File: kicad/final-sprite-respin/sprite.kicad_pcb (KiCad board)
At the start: 4 copper layers, 35 x 35 mm, 70 parts, among them J1 M20-7910442R, U1 CC430F513X, U2 LSM9DS1, U3 SPRITETCXO_TCXO_7Z, U4 DRV8837, U5 ADP5092, U6 DRV8837, U7 DRV8837, U8 TASC, U9 TASC, X1 SPRITEPIN_SPRITE_PIN, X2 SPRITEPIN_SPRITE_PIN

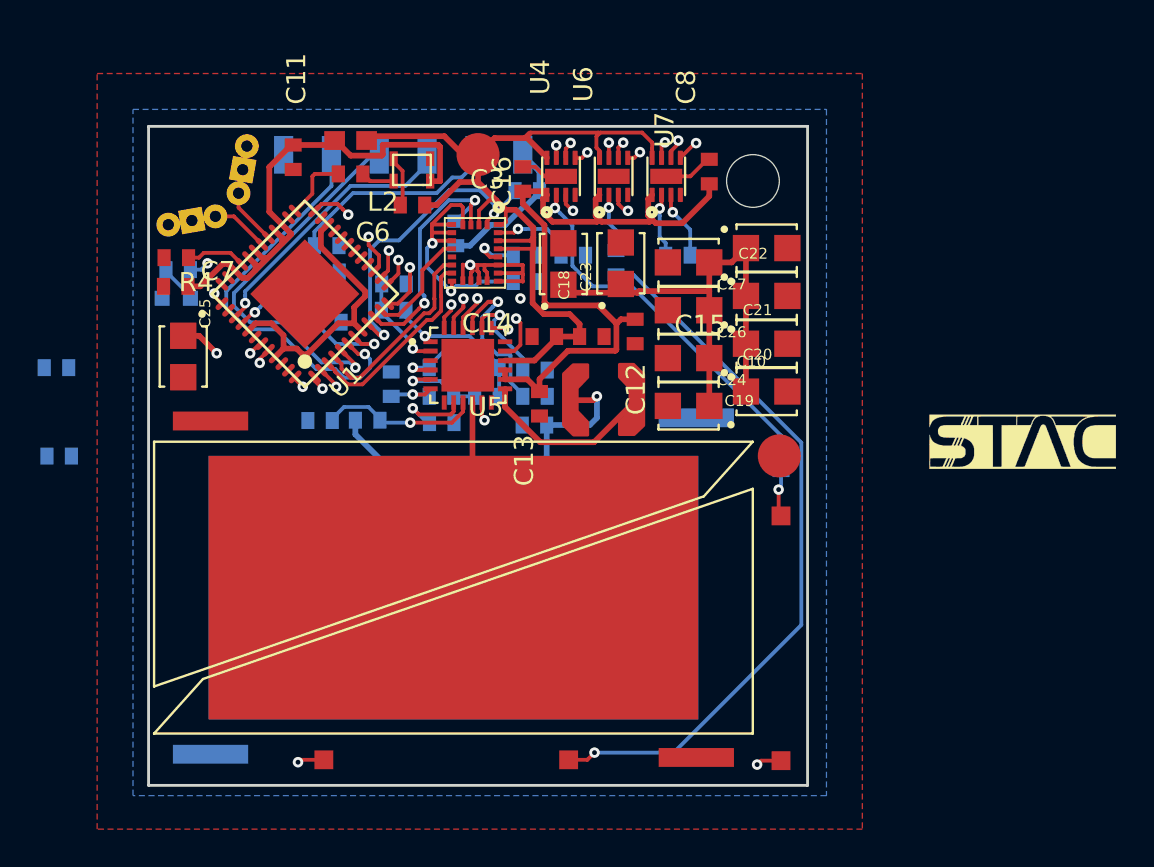
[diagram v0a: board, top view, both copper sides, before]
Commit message: Cap board repsin with all nets connected
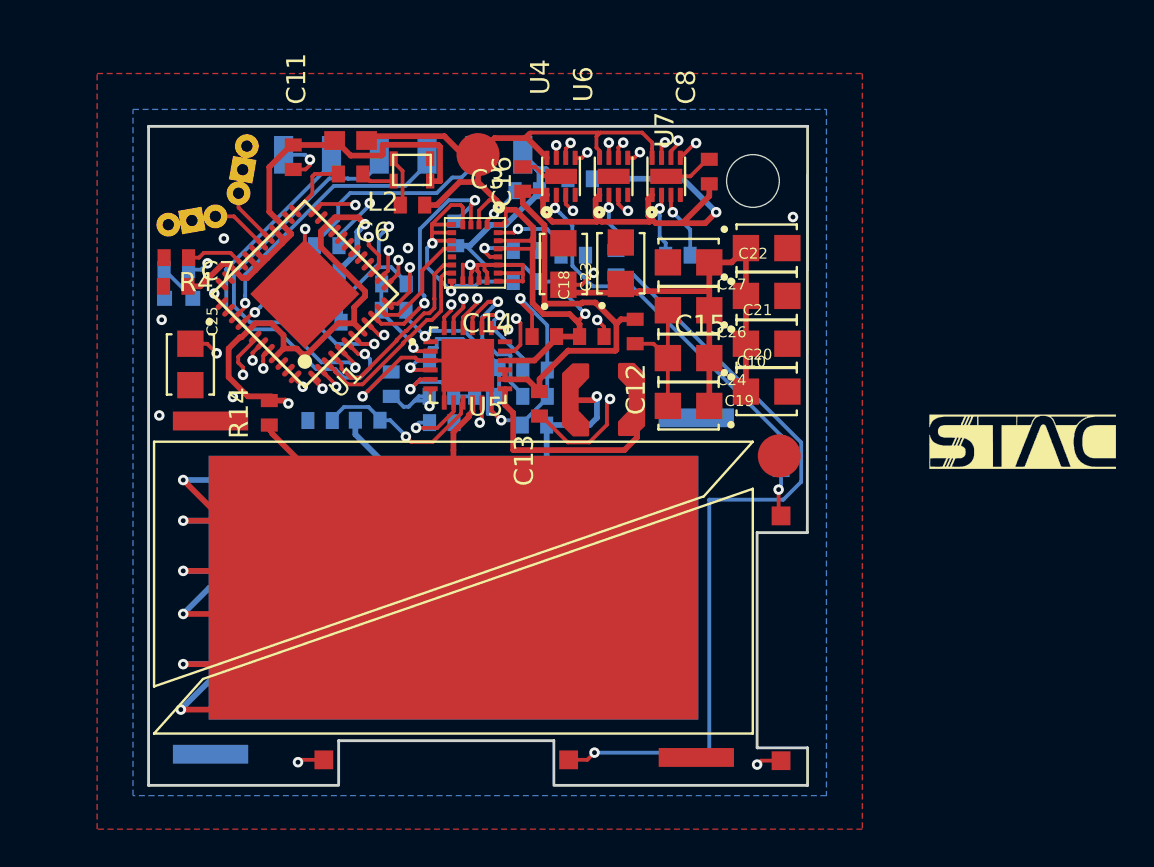
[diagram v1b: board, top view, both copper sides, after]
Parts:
- R14: moved to F.Cu
- moved R13 31.3 mm to (143.8, 86.2)
- moved R14 11.6 mm to (127.3, 98.7), turned to 270 degrees
- moved C25 0.57 mm to (123.1, 96.1)
- moved R21 0.38 mm to (136.4, 95.9)
- moved C4 0.25 mm to (140.9, 90.0)
- moved LED1 0.13 mm to (122.4, 92.6)
- moved R2 0.10 mm to (122.3, 91.1)
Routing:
- net VCCINT: track 38.9 -> 243.3 mm, vias 1 -> 7
- net GND: track 17.9 -> 83.2 mm, vias 2 -> 17
- net VCC: track 71.3 -> 112.9 mm, vias 0 -> 3
- net /VBAT: track 53.5 -> 64.0 mm, vias 2 -> 3
- net VCCIO: track 37.0 -> 46.6 mm, vias 0 -> 1
- net /PGOOD: track 3.65 -> 10.6 mm
- net /PWM2: track 40.3 -> 44.0 mm
- net /PWM1: track 44.3 -> 47.8 mm
- net Net-(L4-Pad1): track 38.5 -> 41.9 mm
- net /SWN: track 9.70 -> 12.3 mm
- net /SCL: track 16.8 -> 14.6 mm
- net /TERM: track 5.24 -> 6.98 mm
- net /SETHYS: track 3.29 -> 4.45 mm
- net /UART_TX: track 20.5 -> 21.4 mm
- net Net-(R7-Pad1): track 8.47 -> 9.34 mm
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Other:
- outline, holes or cut-outs redrawn

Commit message: Fix edge cuts
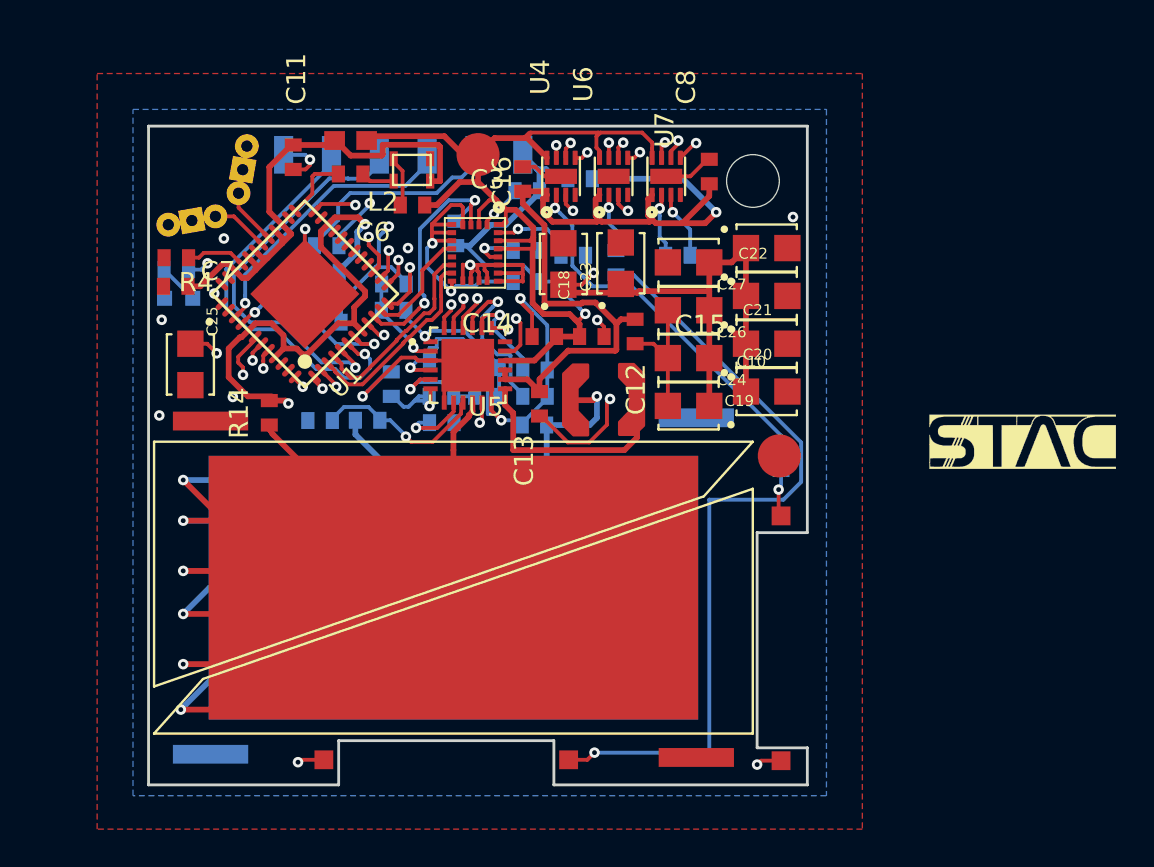
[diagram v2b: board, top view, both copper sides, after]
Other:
- outline, holes or cut-outs redrawn
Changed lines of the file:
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@@
-(kicad_pcb (version 20171130) (host pcbnew "(5.0.0-3-g5ebb6b6)")
+(kicad_pcb (version 20171130) (host pcbnew 6.0.0-rc1-unknown)
   (general
     (thickness 0.7874)
@@
     (2 Route3 signal)
     (31 Bottom signal)
-    (32 B.Adhes user hide)
+    (32 B.Adhes user)
     (33 F.Adhes user)
-    (34 B.Paste user hide)
-    (35 F.Paste user hide)
+    (34 B.Paste user)
+    (35 F.Paste user)
     (36 B.SilkS user)
     (37 F.SilkS user)
-    (38 B.Mask user hide)
-    (39 F.Mask user hide)
-    (40 Dwgs.User user hide)
-    (41 Cmts.User user hide)
-    (42 Eco1.User user hide)
-    (43 Eco2.User user hide)
+    (38 B.Mask user)
+    (39 F.Mask user)
+    (40 Dwgs.User user)
+    (41 Cmts.User user)
+    (42 Eco1.User user)
+    (43 Eco2.User user)
     (44 Edge.Cuts user)
-    (45 Margin user hide)
+    (45 Margin user)
     (46 B.CrtYd user)
     (47 F.CrtYd user)
-    (48 B.Fab user hide)
+    (48 B.Fab user)
     (49 F.Fab user)
   )
@@
     (zone_45_only no)
     (trace_min 0.1524)
-    (segment_width 0.15)
-    (edge_width 0.15)
     (via_size 0.5588)
     (via_drill 0.254)
@@
     (uvia_min_size 0.2)
     (uvia_min_drill 0.1)
+    (edge_width 0.15)
+    (segment_width 0.15)
     (pcb_text_width 0.3)
     (pcb_text_size 1.5 1.5)
@@
     (uvia_dia 25.4)
     (uvia_drill 12.7)
+    (diff_pair_width 0.1524)
     (diff_pair_gap 0.1524)
-    (diff_pair_width 0.1524)
     (add_net /DRDY)
     (add_net /DSW)
@@
     (uvia_dia 25.4)
     (uvia_drill 12.7)
+    (diff_pair_width 0.1524)
     (diff_pair_gap 0.1524)
-    (diff_pair_width 0.1524)
     (add_net /SWN)
     (add_net /VBAT)
@@
     (pad "" np_thru_hole circle (at 0 0) (size 2.8 2.8) (drill 2.8) (layers *.Cu *.Mask))
   )
-  (gr_line (start 130.937 118.452074) (end 120.8411 118.452074) (layer Edge.Cuts) (width 0.15))
-  (gr_line (start 155.8411 116.459) (end 155.8411 118.452074) (layer Edge.Cuts) (width 0.15))
+  (gr_line (start 130.937 118.4275) (end 120.8405 118.4275) (layer Edge.Cuts) (width 0.15))
+  (gr_line (start 155.829 116.459) (end 155.829 118.4275) (layer Edge.Cuts) (width 0.15))
   (gr_line (start 153.162 116.459) (end 155.829 116.459) (layer Edge.Cuts) (width 0.15))
   (gr_line (start 153.162 105.029) (end 153.162 116.459) (layer Edge.Cuts) (width 0.15))
   (gr_line (start 155.829 105.029) (end 153.162 105.029) (layer Edge.Cuts) (width 0.15))
-  (gr_line (start 142.367 116.078) (end 142.367 118.364) (layer Edge.Cuts) (width 0.15))
+  (gr_line (start 142.367 116.078) (end 142.367 118.4275) (layer Edge.Cuts) (width 0.15))
   (gr_line (start 130.937 116.078) (end 142.367 116.078) (layer Edge.Cuts) (width 0.15))
-  (gr_line (start 130.937 118.364) (end 130.937 116.078) (layer Edge.Cuts) (width 0.15))
-  (gr_line (start 155.8411 118.452074) (end 142.367 118.452074) (layer Edge.Cuts) (width 0.15))
+  (gr_line (start 130.937 118.4275) (end 130.937 116.078) (layer Edge.Cuts) (width 0.15))
+  (gr_line (start 155.829 118.4275) (end 142.367 118.4275) (layer Edge.Cuts) (width 0.15))
   (gr_text "STAC Spinor in Space!" (at 135.89 122.428 198) (layer B.SilkS)
     (effects (font (size 1.5 1.5) (thickness 0.3)) (justify mirror))
@@
   )
   (gr_circle (center 153.67 87.884) (end 154.432 88.138) (layer Cmts.User) (width 0.2))
-  (gr_line (start 155.829 105.029) (end 155.8411 83.452074) (layer Edge.Cuts) (width 0.15))
-  (gr_line (start 155.8411 83.452074) (end 120.8411 83.452074) (layer Edge.Cuts) (width 0.15))
-  (gr_line (start 120.8411 83.452074) (end 120.8411 118.452074) (layer Edge.Cuts) (width 0.15))
+  (gr_line (start 155.829 105.029) (end 155.829 83.439) (layer Edge.Cuts) (width 0.15))
+  (gr_line (start 155.829 83.439) (end 120.8405 83.439) (layer Edge.Cuts) (width 0.15))
+  (gr_line (start 120.8405 83.439) (end 120.8405 118.4275) (layer Edge.Cuts) (width 0.15))
   (gr_text "Sprite v2.6" (at 132.616534 115.658071) (layer Dwgs.User)
     (effects (font (size 0.60325 0.60325) (thickness 0.0508)) (justify left bottom mirror))

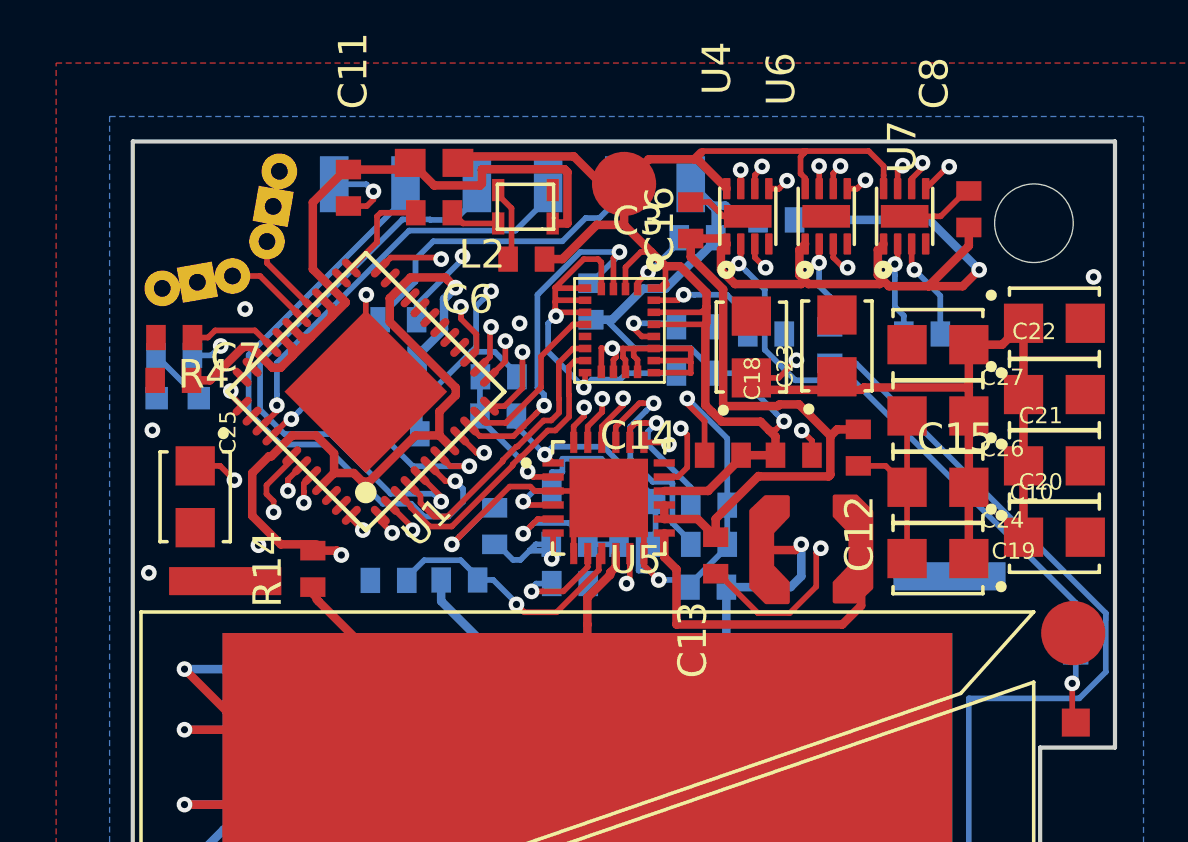
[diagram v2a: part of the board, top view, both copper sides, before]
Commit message: Add via to fix layer 3 fill
While here connect antenna pins to silence unconnected warning.
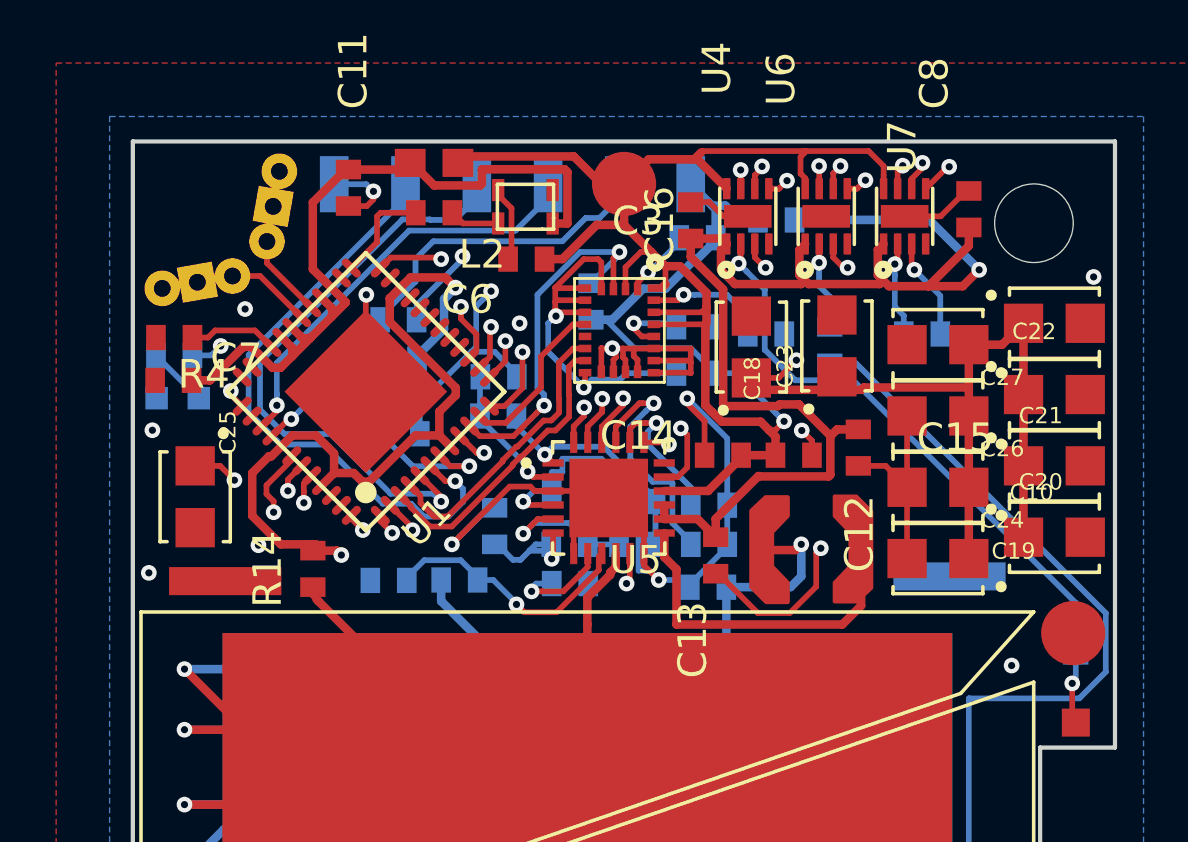
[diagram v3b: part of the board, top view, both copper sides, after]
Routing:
- net /RF_P: track 3.02 -> 5.70 mm
- net /RF_N: track 3.08 -> 5.76 mm
- net GND: vias 17 -> 18
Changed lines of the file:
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@@
     (thickness 0.7874)
     (drawings 24)
-    (tracks 972)
+    (tracks 981)
     (zones 0)
     (modules 70)
@@
   (segment (start 129.1411 92.352074) (end 129.1411 88.9179) (width 0.2032) (layer Top) (net 2))
   (segment (start 141.705 98.836) (end 143.107789 100.238789) (width 0.2032) (layer Top) (net 2))
+  (via (at 152.146 102.108) (size 0.5588) (drill 0.254) (layers Top Bottom) (net 2))
   (segment (start 143.2306 97.9932) (end 144.4498 97.9932) (width 0.3048) (layer Top) (net 3))
   (via (at 144.653 97.79) (size 0.5588) (drill 0.254) (layers Top Bottom) (net 3))
@@
   (segment (start 125.37412 88.231541) (end 124.391806 88.231541) (width 0.2032) (layer Top) (net 35))
   (segment (start 126.857145 89.714566) (end 125.37412 88.231541) (width 0.2032) (layer Top) (net 35))
+  (segment (start 123.361633 88.231541) (end 123.1411 88.452074) (width 0.2032) (layer Top) (net 35))
+  (segment (start 124.391806 88.231541) (end 123.361633 88.231541) (width 0.2032) (layer Top) (net 35))
+  (segment (start 122.110927 88.452074) (end 121.890394 88.672607) (width 0.2032) (layer Top) (net 35))
+  (segment (start 123.1411 88.452074) (end 122.110927 88.452074) (width 0.2032) (layer Top) (net 35))
   (segment (start 125.620567 87.770881) (end 125.620567 87.00278) (width 0.2032) (layer Top) (net 36))
   (segment (start 127.210698 89.361012) (end 125.620567 87.770881) (width 0.2032) (layer Top) (net 36))
+  (segment (start 125.620567 85.972607) (end 125.8411 85.752074) (width 0.2032) (layer Top) (net 36))
+  (segment (start 125.620567 87.00278) (end 125.620567 85.972607) (width 0.2032) (layer Top) (net 36))
+  (segment (start 125.8411 84.721901) (end 126.061633 84.501368) (width 0.2032) (layer Top) (net 36))
+  (segment (start 125.8411 85.752074) (end 125.8411 84.721901) (width 0.2032) (layer Top) (net 36))
   (via (at 129.032 97.282) (size 0.5588) (drill 0.254) (layers Top Bottom) (net 37))
   (segment (start 128.624912 96.874912) (end 129.032 97.282) (width 0.2032) (layer Top) (net 37))

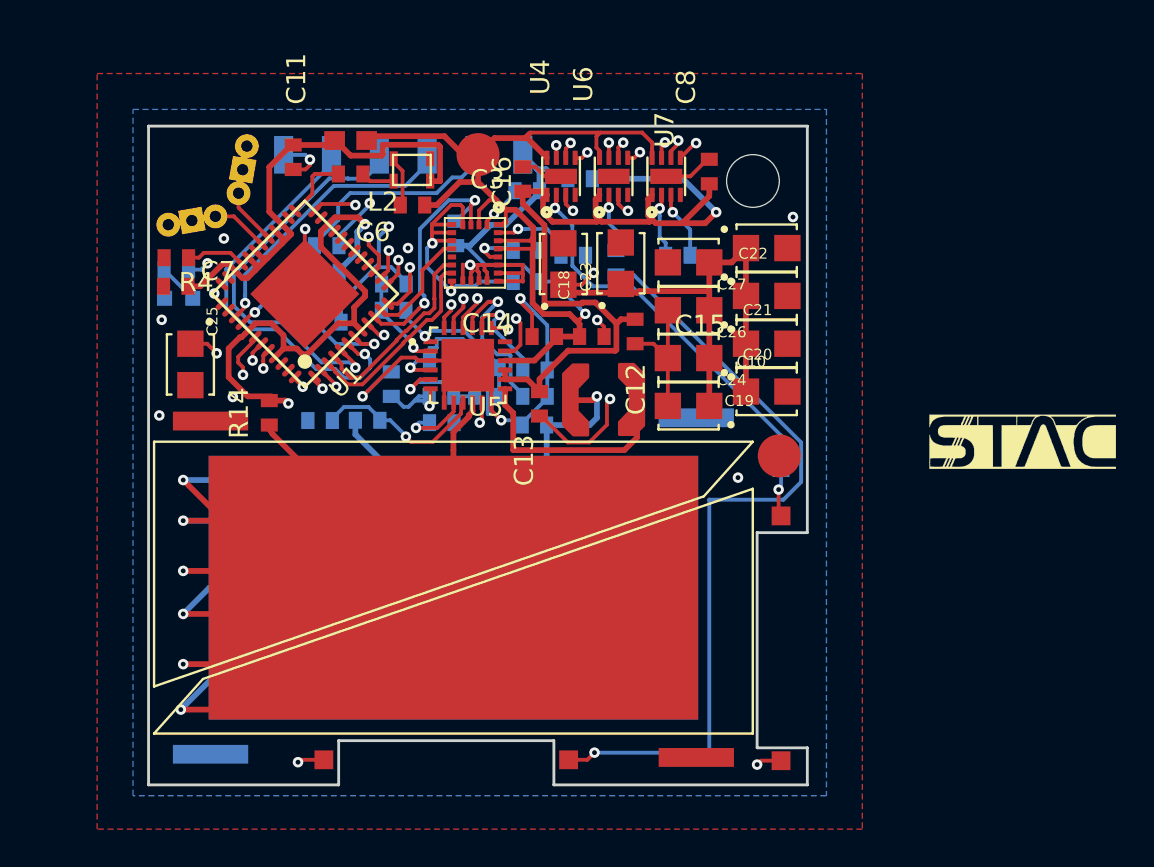
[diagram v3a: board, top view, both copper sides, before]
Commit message: moving around traces to create room for the center spiral inductor
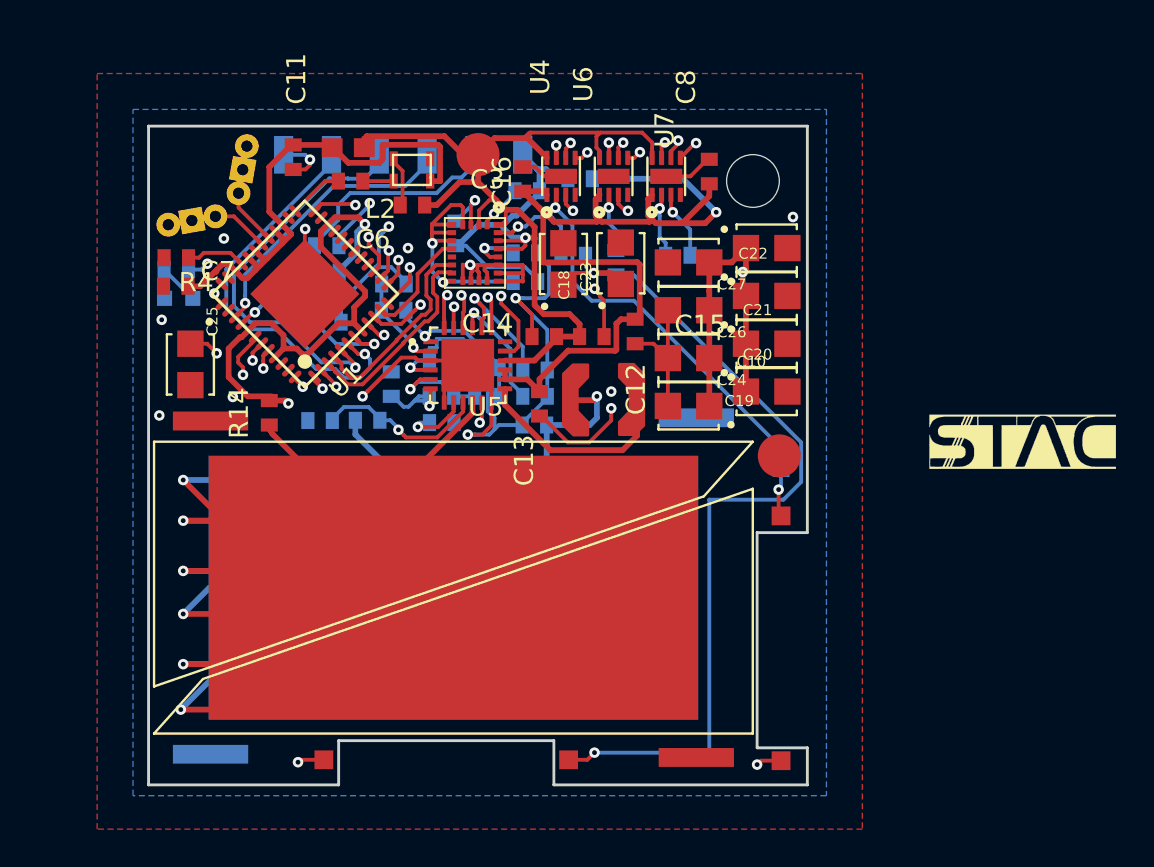
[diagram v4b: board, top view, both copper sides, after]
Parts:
- moved L2 0.40 mm to (131.4, 84.6)
- moved C6 0.38 mm to (131.6, 86.4)
- moved C4 0.13 mm to (140.9, 90.2)
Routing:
- net /PWM2: track 44.0 -> 62.9 mm
- net /PWM1: track 47.8 -> 66.3 mm
- net Net-(L4-Pad2): track 39.3 -> 56.6 mm
- net GND: track 83.2 -> 92.5 mm
- net /SDA: track 13.8 -> 20.6 mm
- net /SCL: track 14.6 -> 21.0 mm
- net /VBAT: track 64.0 -> 68.7 mm, vias 3 -> 4
- net Net-(R10-Pad2): track 9.59 -> 6.36 mm
- net Net-(R9-Pad1): track 5.20 -> 6.70 mm
- net /SWN: track 12.3 -> 11.1 mm
- net Net-(R2-Pad1): track 12.6 -> 13.8 mm
- net VCCINT: track 243.3 -> 244.4 mm
- net VCCIO: track 46.6 -> 47.7 mm
- net Net-(C5-Pad1): track 4.39 -> 5.43 mm
- net /REG_D1: track 10.6 -> 9.75 mm
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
